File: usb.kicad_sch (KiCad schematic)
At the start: 9 parts, among them J7 USB_C_Receptacle_USB2.0, U7 NLAS7242MUTBG

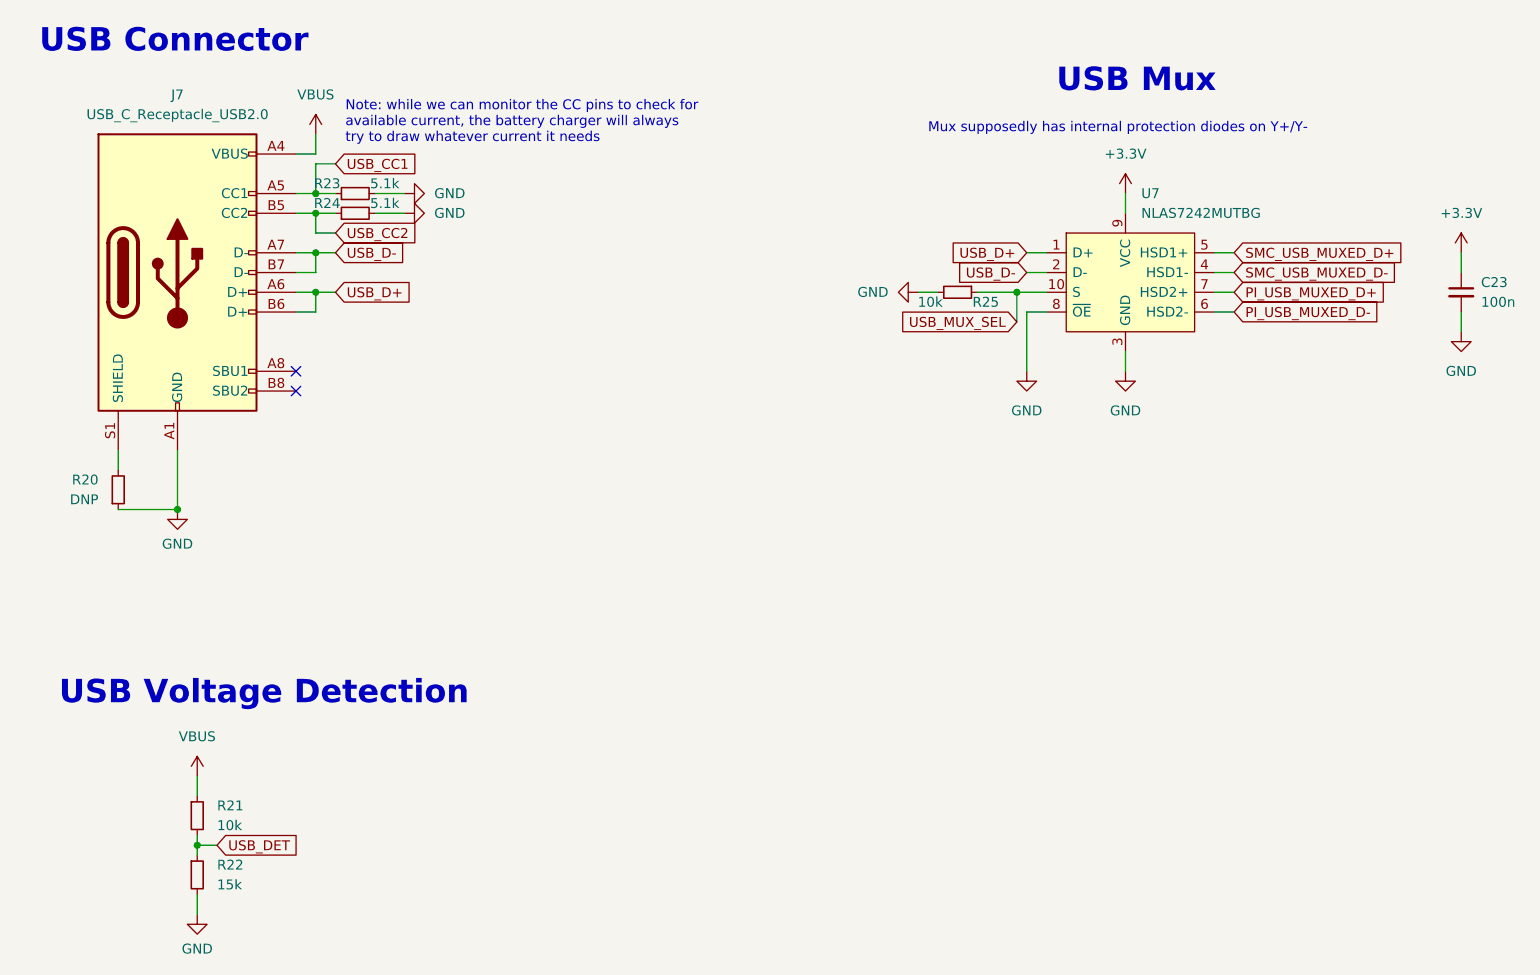
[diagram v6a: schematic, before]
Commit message: layout: preliminary layout of most of board
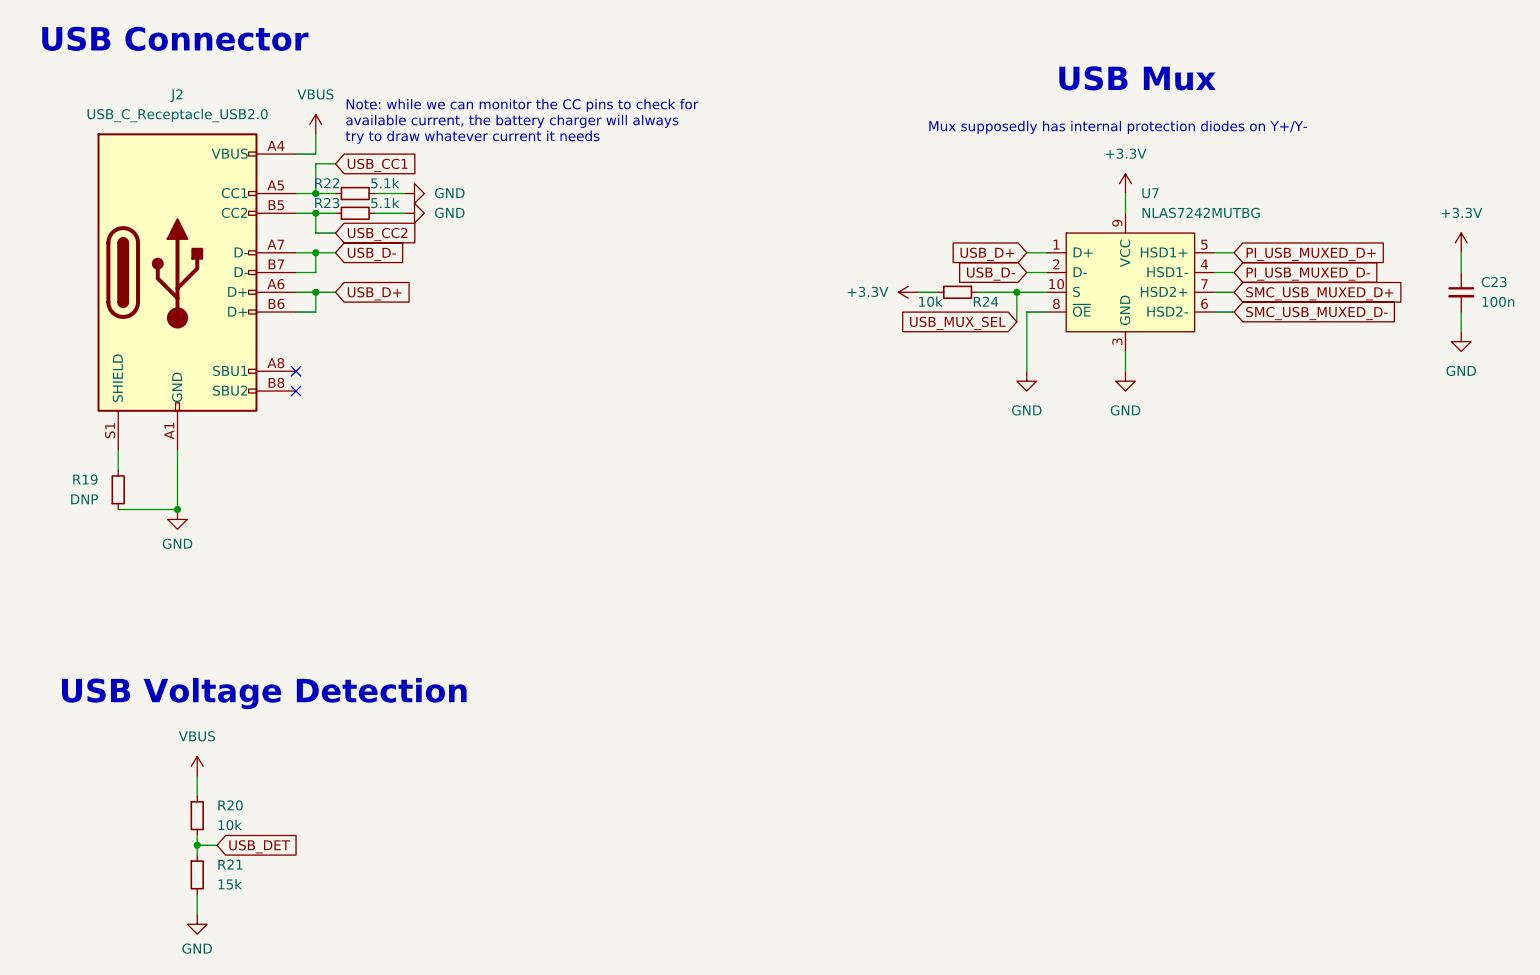
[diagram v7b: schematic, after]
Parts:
- renumbered J7 to J2, R20 to R19, R21 to R20, R22 to R21, R23 to R22, R24 to R23, R25 to R24
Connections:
- net +3V3: now also R24.2
- net GND: no longer R24.2
- net PI_USB_MUXED_D+: now also U7.5 (HSD1+); no longer U7.7 (HSD2+)
- net PI_USB_MUXED_D-: now also U7.4 (HSD1-); no longer U7.6 (HSD2-)
- net SMC_USB_MUXED_D+: now also U7.7 (HSD2+); no longer U7.5 (HSD1+)
- net SMC_USB_MUXED_D-: now also U7.6 (HSD2-); no longer U7.4 (HSD1-)
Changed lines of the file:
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@@
     (effects (font (size 1.27 1.27)) (justify left bottom))
   )
-  (global_label "SMC_USB_MUXED_D+" (shape input) (at 199.39 77.47 0) (fields_autoplaced)
-    (effects (font (size 1.27 1.27)) (justify left))
-    (property "Intersheet References" "${INTERSHEET_REFS}" (id 0) (at 221.6998 77.3906 0)
-      (effects (font (size 1.27 1.27)) (justify left) hide)
-    )
-  )
-  (global_label "PI_USB_MUXED_D+" (shape input) (at 199.39 82.55 0) (fields_autoplaced)
-    (effects (font (size 1.27 1.27)) (justify left))
-    (property "Intersheet References" "${INTERSHEET_REFS}" (id 0) (at 219.6436 82.4706 0)
+  (global_label "SMC_USB_MUXED_D+" (shape input) (at 199.39 82.55 0) (fields_autoplaced)
+    (effects (font (size 1.27 1.27)) (justify left))
+    (property "Intersheet References" "${INTERSHEET_REFS}" (id 0) (at 221.6998 82.4706 0)
+      (effects (font (size 1.27 1.27)) (justify left) hide)
+    )
+  )
+  (global_label "PI_USB_MUXED_D+" (shape input) (at 199.39 77.47 0) (fields_autoplaced)
+    (effects (font (size 1.27 1.27)) (justify left))
+    (property "Intersheet References" "${INTERSHEET_REFS}" (id 0) (at 219.6436 77.3906 0)
       (effects (font (size 1.27 1.27)) (justify left) hide)
     )
@@
     )
   )
-  (global_label "SMC_USB_MUXED_D-" (shape input) (at 199.39 80.01 0) (fields_autoplaced)
-    (effects (font (size 1.27 1.27)) (justify left))
-    (property "Intersheet References" "${INTERSHEET_REFS}" (id 0) (at 221.6998 79.9306 0)
+  (global_label "SMC_USB_MUXED_D-" (shape input) (at 199.39 85.09 0) (fields_autoplaced)
+    (effects (font (size 1.27 1.27)) (justify left))
+    (property "Intersheet References" "${INTERSHEET_REFS}" (id 0) (at 221.6998 85.0106 0)
       (effects (font (size 1.27 1.27)) (justify left) hide)
     )
@@
     )
   )
-  (global_label "PI_USB_MUXED_D-" (shape input) (at 199.39 85.09 0) (fields_autoplaced)
-    (effects (font (size 1.27 1.27)) (justify left))
-    (property "Intersheet References" "${INTERSHEET_REFS}" (id 0) (at 219.6436 85.0106 0)
+  (global_label "PI_USB_MUXED_D-" (shape input) (at 199.39 80.01 0) (fields_autoplaced)
+    (effects (font (size 1.27 1.27)) (justify left))
+    (property "Intersheet References" "${INTERSHEET_REFS}" (id 0) (at 219.6436 79.9306 0)
       (effects (font (size 1.27 1.27)) (justify left) hide)
     )
@@
   (symbol (lib_id "power:+3.3V") (at 228.6 77.47 0) (unit 1)
     (in_bom yes) (on_board yes) (fields_autoplaced)
-    (property "Reference" "#PWR0116" (id 0) (at 228.6 81.28 0)
+    (property "Reference" "#PWR062" (id 0) (at 228.6 81.28 0)
       (effects (font (size 1.27 1.27)) hide)
     )
@@
   (symbol (lib_id "power:GND") (at 66.04 162.56 0) (unit 1)
     (in_bom yes) (on_board yes) (fields_autoplaced)
-    (property "Reference" "#PWR051" (id 0) (at 66.04 168.91 0)
+    (property "Reference" "#PWR054" (id 0) (at 66.04 168.91 0)
       (effects (font (size 1.27 1.27)) hide)
     )
@@
   (symbol (lib_id "Device:R_Small") (at 66.04 157.48 0) (unit 1)
     (in_bom yes) (on_board yes) (fields_autoplaced)
-    (property "Reference" "R22" (id 0) (at 68.58 156.2099 0)
+    (property "Reference" "R21" (id 0) (at 68.58 156.2099 0)
       (effects (font (size 1.27 1.27)) (justify left))
     )
@@
   (symbol (lib_id "Device:R_Small") (at 163.83 82.55 270) (unit 1)
     (in_bom yes) (on_board yes)
-    (property "Reference" "R25" (id 0) (at 165.735 83.82 90)
+    (property "Reference" "R24" (id 0) (at 165.735 83.82 90)
       (effects (font (size 1.27 1.27)) (justify left))
     )
@@
   (symbol (lib_id "Device:R_Small") (at 66.04 149.86 0) (unit 1)
     (in_bom yes) (on_board yes) (fields_autoplaced)
-    (property "Reference" "R21" (id 0) (at 68.58 148.5899 0)
+    (property "Reference" "R20" (id 0) (at 68.58 148.5899 0)
       (effects (font (size 1.27 1.27)) (justify left))
     )
@@
   (symbol (lib_id "power:VBUS") (at 66.04 144.78 0) (unit 1)
     (in_bom yes) (on_board yes) (fields_autoplaced)
-    (property "Reference" "#PWR050" (id 0) (at 66.04 148.59 0)
+    (property "Reference" "#PWR053" (id 0) (at 66.04 148.59 0)
       (effects (font (size 1.27 1.27)) hide)
     )
@@
   (symbol (lib_id "Device:R_Small") (at 86.36 69.85 90) (unit 1)
     (in_bom yes) (on_board yes)
-    (property "Reference" "R23" (id 0) (at 84.455 68.58 90)
+    (property "Reference" "R22" (id 0) (at 84.455 68.58 90)
       (effects (font (size 1.27 1.27)) (justify left))
     )
@@
   (symbol (lib_id "power:VBUS") (at 81.28 62.23 0) (unit 1)
     (in_bom yes) (on_board yes) (fields_autoplaced)
-    (property "Reference" "#PWR052" (id 0) (at 81.28 66.04 0)
+    (property "Reference" "#PWR055" (id 0) (at 81.28 66.04 0)
       (effects (font (size 1.27 1.27)) hide)
     )
@@
   (symbol (lib_id "power:GND") (at 92.71 69.85 90) (unit 1)
     (in_bom yes) (on_board yes) (fields_autoplaced)
-    (property "Reference" "#PWR053" (id 0) (at 99.06 69.85 0)
+    (property "Reference" "#PWR056" (id 0) (at 99.06 69.85 0)
       (effects (font (size 1.27 1.27)) hide)
     )
@@
   (symbol (lib_id "power:GND") (at 92.71 72.39 90) (unit 1)
     (in_bom yes) (on_board yes) (fields_autoplaced)
-    (property "Reference" "#PWR054" (id 0) (at 99.06 72.39 0)
+    (property "Reference" "#PWR057" (id 0) (at 99.06 72.39 0)
       (effects (font (size 1.27 1.27)) hide)
     )
@@
   (symbol (lib_id "power:GND") (at 228.6 87.63 0) (unit 1)
     (in_bom yes) (on_board yes) (fields_autoplaced)
-    (property "Reference" "#PWR0117" (id 0) (at 228.6 93.98 0)
+    (property "Reference" "#PWR063" (id 0) (at 228.6 93.98 0)
       (effects (font (size 1.27 1.27)) hide)
     )
@@
   (symbol (lib_id "power:GND") (at 172.72 92.71 0) (unit 1)
     (in_bom yes) (on_board yes) (fields_autoplaced)
-    (property "Reference" "#PWR0130" (id 0) (at 172.72 99.06 0)
+    (property "Reference" "#PWR059" (id 0) (at 172.72 99.06 0)
       (effects (font (size 1.27 1.27)) hide)
     )
@@
   (symbol (lib_id "Device:R_Small") (at 86.36 72.39 90) (unit 1)
     (in_bom yes) (on_board yes)
-    (property "Reference" "R24" (id 0) (at 84.455 71.12 90)
+    (property "Reference" "R23" (id 0) (at 84.455 71.12 90)
       (effects (font (size 1.27 1.27)) (justify left))
     )
@@
   (symbol (lib_id "power:GND") (at 185.42 92.71 0) (unit 1)
     (in_bom yes) (on_board yes) (fields_autoplaced)
-    (property "Reference" "#PWR0128" (id 0) (at 185.42 99.06 0)
+    (property "Reference" "#PWR061" (id 0) (at 185.42 99.06 0)
       (effects (font (size 1.27 1.27)) hide)
     )
@@
     (pin "1")
   )
+  (symbol (lib_id "power:+3.3V") (at 158.75 82.55 90) (unit 1)
+    (in_bom yes) (on_board yes) (fields_autoplaced)
+    (property "Reference" "#PWR0135" (id 0) (at 162.56 82.55 0)
+      (effects (font (size 1.27 1.27)) hide)
+    )
+    (property "Value" "+3.3V" (id 1) (at 154.94 82.5499 90)
+      (effects (font (size 1.27 1.27)) (justify left))
+    )
+    (property "Footprint" "" (id 2) (at 158.75 82.55 0)
+      (effects (font (size 1.27 1.27)) hide)
+    )
+    (property "Datasheet" "" (id 3) (at 158.75 82.55 0)
+      (effects (font (size 1.27 1.27)) hide)
+    )
+    (pin "1")
+  )
   (symbol (lib_id "power:GND") (at 63.5 110.49 0) (unit 1)
     (in_bom yes) (on_board yes) (fields_autoplaced)
-    (property "Reference" "#PWR049" (id 0) (at 63.5 116.84 0)
+    (property "Reference" "#PWR052" (id 0) (at 63.5 116.84 0)
       (effects (font (size 1.27 1.27)) hide)
     )
@@
   (symbol (lib_id "Connector:USB_C_Receptacle_USB2.0") (at 63.5 80.01 0) (unit 1)
     (in_bom yes) (on_board yes) (fields_autoplaced)
-    (property "Reference" "J7" (id 0) (at 63.5 57.15 0))
+    (property "Reference" "J2" (id 0) (at 63.5 57.15 0))
     (property "Value" "USB_C_Receptacle_USB2.0" (id 1) (at 63.5 59.69 0))
     (property "Footprint" "Gigahawk:USB_C_Receptacle_GCT_USB4085" (id 2) (at 67.31 80.01 0)
@@
   (symbol (lib_id "power:+3.3V") (at 185.42 69.85 0) (unit 1)
     (in_bom yes) (on_board yes) (fields_autoplaced)
-    (property "Reference" "#PWR0129" (id 0) (at 185.42 73.66 0)
+    (property "Reference" "#PWR060" (id 0) (at 185.42 73.66 0)
       (effects (font (size 1.27 1.27)) hide)
     )
@@
     (pin "1")
   )
-  (symbol (lib_id "power:GND") (at 158.75 82.55 270) (unit 1)
-    (in_bom yes) (on_board yes) (fields_autoplaced)
-    (property "Reference" "#PWR0118" (id 0) (at 152.4 82.55 0)
-      (effects (font (size 1.27 1.27)) hide)
-    )
-    (property "Value" "GND" (id 1) (at 154.94 82.5499 90)
-      (effects (font (size 1.27 1.27)) (justify right))
-    )
-    (property "Footprint" "" (id 2) (at 158.75 82.55 0)
-      (effects (font (size 1.27 1.27)) hide)
-    )
-    (property "Datasheet" "" (id 3) (at 158.75 82.55 0)
-      (effects (font (size 1.27 1.27)) hide)
-    )
-    (pin "1")
-  )
   (symbol (lib_id "Device:R_Small") (at 55.88 107.95 0) (mirror x) (unit 1)
     (in_bom yes) (on_board yes) (fields_autoplaced)
-    (property "Reference" "R20" (id 0) (at 53.34 106.6799 0)
-      (effects (font (size 1.27 1.27)) (justify right))
-    )
+    (property "Reference" "R19" (id 0) (at 53.34 106.6799 0)
+      (effects (font (size 1.27 1.27)) (justify right))
+    )

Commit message: layout, routing: relayout and reroute board
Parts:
- C23: value 100n -> (none); footprint Capacitor_SMD:C_0402_1005Metric -> (none)
- J2: value USB_C_Receptacle_USB2.0 -> (none); footprint Gigahawk:USB_C_Receptacle_GCT_USB4085 -> (none)
- R19: value DNP -> (none); footprint Resistor_SMD:R_0402_1005Metric -> (none)
- R20, R24: value 10k -> (none); footprint Resistor_SMD:R_0402_1005Metric -> (none)
- R21: value 15k -> (none); footprint Resistor_SMD:R_0402_1005Metric -> (none)
- R22, R23: value 5.1k -> (none); footprint Resistor_SMD:R_0402_1005Metric -> (none)
- U7: value NLAS7242MUTBG -> (none); footprint Package_DFN_QFN:UQFN-10_1.4x1.8mm_P0.4mm -> (none)
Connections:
- net USB_SHIELD: now reaches J2.S1 (SHIELD), R19.2
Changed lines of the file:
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@@
     (effects (font (size 1.27 1.27)) (justify left bottom))
+  )
+  (label "USB_SHIELD" (at 55.88 104.14 180)
+    (effects (font (size 1.27 1.27)) (justify right bottom))
   )
   (global_label "SMC_USB_MUXED_D+" (shape input) (at 199.39 82.55 0) (fields_autoplaced)
@@
       (effects (font (size 1.27 1.27)) (justify left))
     )
-    (property "Value" "15k" (id 1) (at 68.58 158.7499 0)
-      (effects (font (size 1.27 1.27)) (justify left))
-    )
-    (property "Footprint" "Resistor_SMD:R_0402_1005Metric" (id 2) (at 66.04 157.48 0)
+    (property "Value" "" (id 1) (at 68.58 158.7499 0)
+      (effects (font (size 1.27 1.27)) (justify left))
+    )
+    (property "Footprint" "" (id 2) (at 66.04 157.48 0)
       (effects (font (size 1.27 1.27)) hide)
     )
@@
       (effects (font (size 1.27 1.27)) (justify left))
     )
-    (property "Value" "10k" (id 1) (at 161.925 83.82 90)
-      (effects (font (size 1.27 1.27)) (justify right))
-    )
-    (property "Footprint" "Resistor_SMD:R_0402_1005Metric" (id 2) (at 163.83 82.55 0)
+    (property "Value" "" (id 1) (at 161.925 83.82 90)
+      (effects (font (size 1.27 1.27)) (justify right))
+    )
+    (property "Footprint" "" (id 2) (at 163.83 82.55 0)
       (effects (font (size 1.27 1.27)) hide)
     )
@@
       (effects (font (size 1.27 1.27)) (justify left))
     )
-    (property "Value" "10k" (id 1) (at 68.58 151.1299 0)
-      (effects (font (size 1.27 1.27)) (justify left))
-    )
-    (property "Footprint" "Resistor_SMD:R_0402_1005Metric" (id 2) (at 66.04 149.86 0)
+    (property "Value" "" (id 1) (at 68.58 151.1299 0)
+      (effects (font (size 1.27 1.27)) (justify left))
+    )
+    (property "Footprint" "" (id 2) (at 66.04 149.86 0)
       (effects (font (size 1.27 1.27)) hide)
     )
@@
       (effects (font (size 1.27 1.27)) (justify left))
     )
-    (property "Value" "5.1k" (id 1) (at 88.265 68.58 90)
-      (effects (font (size 1.27 1.27)) (justify right))
-    )
-    (property "Footprint" "Resistor_SMD:R_0402_1005Metric" (id 2) (at 86.36 69.85 0)
+    (property "Value" "" (id 1) (at 88.265 68.58 90)
+      (effects (font (size 1.27 1.27)) (justify right))
+    )
+    (property "Footprint" "" (id 2) (at 86.36 69.85 0)
       (effects (font (size 1.27 1.27)) hide)
     )
@@
       (effects (font (size 1.27 1.27)) (justify left))
     )
-    (property "Value" "NLAS7242MUTBG" (id 1) (at 187.4394 72.39 0)
-      (effects (font (size 1.27 1.27)) (justify left))
-    )
-    (property "Footprint" "Package_DFN_QFN:UQFN-10_1.4x1.8mm_P0.4mm" (id 2) (at 167.64 64.77 0)
+    (property "Value" "" (id 1) (at 187.4394 72.39 0)
+      (effects (font (size 1.27 1.27)) (justify left))
+    )
+    (property "Footprint" "" (id 2) (at 167.64 64.77 0)
       (effects (font (size 1.27 1.27)) (justify left) hide)
     )
@@
       (effects (font (size 1.27 1.27)) (justify left))
     )
-    (property "Value" "100n" (id 1) (at 231.14 83.8262 0)
-      (effects (font (size 1.27 1.27)) (justify left))
-    )
-    (property "Footprint" "Capacitor_SMD:C_0402_1005Metric" (id 2) (at 228.6 82.55 0)
+    (property "Value" "" (id 1) (at 231.14 83.8262 0)
+      (effects (font (size 1.27 1.27)) (justify left))
+    )
+    (property "Footprint" "" (id 2) (at 228.6 82.55 0)
       (effects (font (size 1.27 1.27)) hide)
     )
@@
       (effects (font (size 1.27 1.27)) (justify left))
     )
-    (property "Value" "5.1k" (id 1) (at 88.265 71.12 90)
-      (effects (font (size 1.27 1.27)) (justify right))
-    )
-    (property "Footprint" "Resistor_SMD:R_0402_1005Metric" (id 2) (at 86.36 72.39 0)
+    (property "Value" "" (id 1) (at 88.265 71.12 90)
+      (effects (font (size 1.27 1.27)) (justify right))
+    )
+    (property "Footprint" "" (id 2) (at 86.36 72.39 0)
       (effects (font (size 1.27 1.27)) hide)
     )
@@
     (in_bom yes) (on_board yes) (fields_autoplaced)
     (property "Reference" "J2" (id 0) (at 63.5 57.15 0))
-    (property "Value" "USB_C_Receptacle_USB2.0" (id 1) (at 63.5 59.69 0))
-    (property "Footprint" "Gigahawk:USB_C_Receptacle_GCT_USB4085" (id 2) (at 67.31 80.01 0)
+    (property "Value" "" (id 1) (at 63.5 59.69 0))
+    (property "Footprint" "" (id 2) (at 67.31 80.01 0)
       (effects (font (size 1.27 1.27)) hide)
     )
@@
       (effects (font (size 1.27 1.27)) (justify right))
     )
-    (property "Value" "DNP" (id 1) (at 53.34 109.2199 0)
-      (effects (font (size 1.27 1.27)) (justify right))
-    )
-    (property "Footprint" "Resistor_SMD:R_0402_1005Metric" (id 2) (at 55.88 107.95 0)
-      (effects (font (size 1.27 1.27)) hide)
-    )
+    (property "Value" "" (id 1) (at 53.34 109.2199 0)
+      (effects (font (size 1.27 1.27)) (justify right))
+    )
+    (property "Footprint" "" (id 2) (at 55.88 107.95 0)
+      (effects (font (size 1.27 1.27)) hide)
+    )
